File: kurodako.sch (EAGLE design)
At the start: 41 parts, among them J1 CONN-4P-MICROMATCH-SMD, J10 CONN-4P-MICROMATCH-SMD, J11 CONN-4P-MICROMATCH-SMD, J12 CONN-4P-MICROMATCH-SMD, J13 CONN-4P-MICROMATCH-SMD, J14 CONN-4P-MICROMATCH-SMD, J15 CONN-4P-MICROMATCH-SMD, J16 CONN-4P-MICROMATCH-SMD, J2 CONN-4P-MICROMATCH-SMD, J3 CONN-4P-MICROMATCH-SMD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

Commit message: Added resistors on mic high and possiblity to change pdm clk.
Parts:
- added R10, R11, R12, R13: 100, adafruit:R-US_R0805
- added R9: (no value), adafruit:R-US_R0805
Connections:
- new net DAT1_H: J1.3, J2.3, MIC1L.DAT, R10.2
- new net DAT2_H: J5.3, J6.3, MIC2L.DAT, R11.2
- new net DAT3_H: J10.3, J9.3, MIC3L.DAT, R12.2
- new net DAT4_H: J13.3, J14.3, MIC4L.DAT, R13.2
- net DAT1: now also R10.1; no longer J1.3, J2.3, MIC1L.DAT
- net DAT2: now also R11.1; no longer J5.3, J6.3, MIC2L.DAT
- net DAT3: now also R12.1; no longer J10.3, J9.3, MIC3L.DAT
- net DAT4: now also R13.1; no longer J13.3, J14.3, MIC4L.DAT
- net PDM_CLK: now also R9.1, R9.2

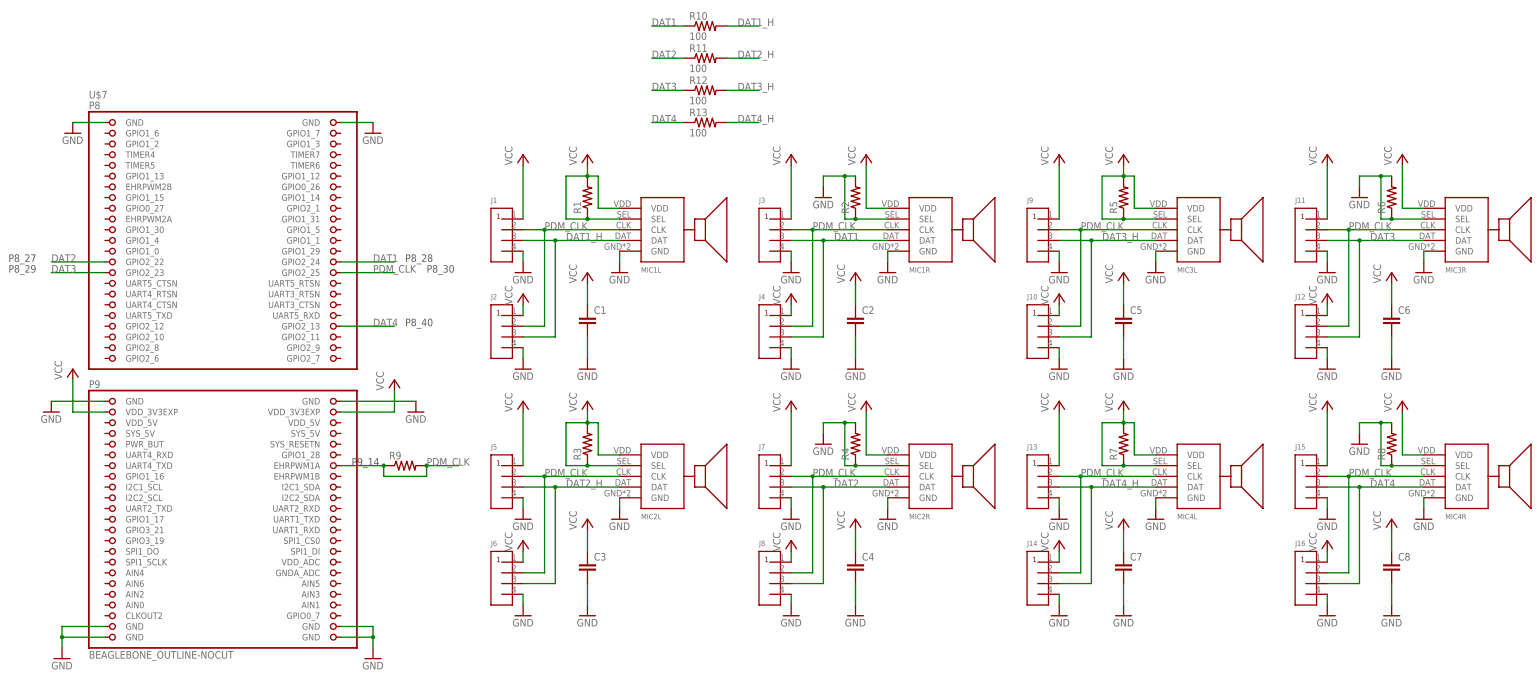
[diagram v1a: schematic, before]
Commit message: Added some values for the components on the schematics, a pdf of the schematics and the BOM.
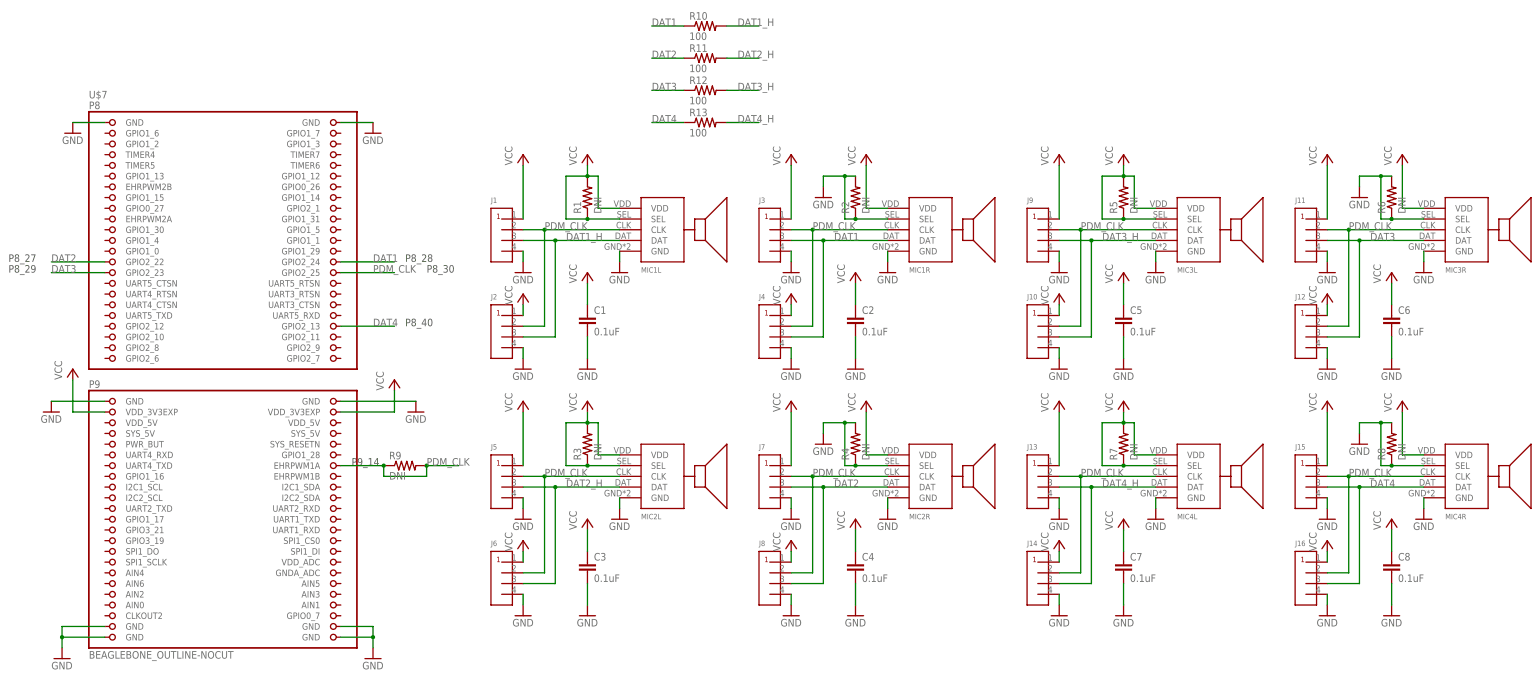
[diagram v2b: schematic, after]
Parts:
- C1, C2, C3, C4, C5, C6, C7, C8: value (none) -> 0.1uF
- R1, R2, R3, R4, R5, R6, R7, R8, R9: value (none) -> DNI
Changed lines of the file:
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@@
 <part name="J1" library="LCAV" deviceset="CONN-4P" device="-MICROMATCH-SMD"/>
 <part name="J2" library="LCAV" deviceset="CONN-4P" device="-MICROMATCH-SMD"/>
-<part name="R1" library="adafruit" deviceset="R-US_" device="R0805"/>
+<part name="R1" library="adafruit" deviceset="R-US_" device="R0805" value="DNI"/>
 <part name="GND1" library="supply1" deviceset="GND" device=""/>
 <part name="P+1" library="supply1" deviceset="VCC" device=""/>
-<part name="C1" library="SparkFun" deviceset="CAP" device="0805"/>
+<part name="C1" library="SparkFun" deviceset="CAP" device="0805" value="0.1uF"/>
 <part name="GND2" library="supply1" deviceset="GND" device=""/>
 <part name="GND4" library="supply1" deviceset="GND" device=""/>
@@
 <part name="J3" library="LCAV" deviceset="CONN-4P" device="-MICROMATCH-SMD"/>
 <part name="J4" library="LCAV" deviceset="CONN-4P" device="-MICROMATCH-SMD"/>
-<part name="R2" library="adafruit" deviceset="R-US_" device="R0805"/>
+<part name="R2" library="adafruit" deviceset="R-US_" device="R0805" value="DNI"/>
 <part name="GND3" library="supply1" deviceset="GND" device=""/>
 <part name="P+3" library="supply1" deviceset="VCC" device=""/>
-<part name="C2" library="SparkFun" deviceset="CAP" device="0805"/>
+<part name="C2" library="SparkFun" deviceset="CAP" device="0805" value="0.1uF"/>
 <part name="GND6" library="supply1" deviceset="GND" device=""/>
 <part name="GND7" library="supply1" deviceset="GND" device=""/>
@@
 <part name="J5" library="LCAV" deviceset="CONN-4P" device="-MICROMATCH-SMD"/>
 <part name="J6" library="LCAV" deviceset="CONN-4P" device="-MICROMATCH-SMD"/>
-<part name="R3" library="adafruit" deviceset="R-US_" device="R0805"/>
+<part name="R3" library="adafruit" deviceset="R-US_" device="R0805" value="DNI"/>
 <part name="GND10" library="supply1" deviceset="GND" device=""/>
 <part name="P+7" library="supply1" deviceset="VCC" device=""/>
-<part name="C3" library="SparkFun" deviceset="CAP" device="0805"/>
+<part name="C3" library="SparkFun" deviceset="CAP" device="0805" value="0.1uF"/>
 <part name="GND11" library="supply1" deviceset="GND" device=""/>
 <part name="GND12" library="supply1" deviceset="GND" device=""/>
@@
 <part name="J7" library="LCAV" deviceset="CONN-4P" device="-MICROMATCH-SMD"/>
 <part name="J8" library="LCAV" deviceset="CONN-4P" device="-MICROMATCH-SMD"/>
-<part name="R4" library="adafruit" deviceset="R-US_" device="R0805"/>
+<part name="R4" library="adafruit" deviceset="R-US_" device="R0805" value="DNI"/>
 <part name="GND14" library="supply1" deviceset="GND" device=""/>
 <part name="P+10" library="supply1" deviceset="VCC" device=""/>
-<part name="C4" library="SparkFun" deviceset="CAP" device="0805"/>
+<part name="C4" library="SparkFun" deviceset="CAP" device="0805" value="0.1uF"/>
 <part name="GND15" library="supply1" deviceset="GND" device=""/>
 <part name="GND16" library="supply1" deviceset="GND" device=""/>
@@
 <part name="J9" library="LCAV" deviceset="CONN-4P" device="-MICROMATCH-SMD"/>
 <part name="J10" library="LCAV" deviceset="CONN-4P" device="-MICROMATCH-SMD"/>
-<part name="R5" library="adafruit" deviceset="R-US_" device="R0805"/>
+<part name="R5" library="adafruit" deviceset="R-US_" device="R0805" value="DNI"/>
 <part name="GND19" library="supply1" deviceset="GND" device=""/>
 <part name="P+13" library="supply1" deviceset="VCC" device=""/>
-<part name="C5" library="SparkFun" deviceset="CAP" device="0805"/>
+<part name="C5" library="SparkFun" deviceset="CAP" device="0805" value="0.1uF"/>
 <part name="GND20" library="supply1" deviceset="GND" device=""/>
 <part name="GND21" library="supply1" deviceset="GND" device=""/>
@@
 <part name="J11" library="LCAV" deviceset="CONN-4P" device="-MICROMATCH-SMD"/>
 <part name="J12" library="LCAV" deviceset="CONN-4P" device="-MICROMATCH-SMD"/>
-<part name="R6" library="adafruit" deviceset="R-US_" device="R0805"/>
+<part name="R6" library="adafruit" deviceset="R-US_" device="R0805" value="DNI"/>
 <part name="GND23" library="supply1" deviceset="GND" device=""/>
 <part name="P+16" library="supply1" deviceset="VCC" device=""/>
-<part name="C6" library="SparkFun" deviceset="CAP" device="0805"/>
+<part name="C6" library="SparkFun" deviceset="CAP" device="0805" value="0.1uF"/>
 <part name="GND24" library="supply1" deviceset="GND" device=""/>
 <part name="GND25" library="supply1" deviceset="GND" device=""/>
@@
 <part name="J13" library="LCAV" deviceset="CONN-4P" device="-MICROMATCH-SMD"/>
 <part name="J14" library="LCAV" deviceset="CONN-4P" device="-MICROMATCH-SMD"/>
-<part name="R7" library="adafruit" deviceset="R-US_" device="R0805"/>
+<part name="R7" library="adafruit" deviceset="R-US_" device="R0805" value="DNI"/>
 <part name="GND28" library="supply1" deviceset="GND" device=""/>
 <part name="P+19" library="supply1" deviceset="VCC" device=""/>
-<part name="C7" library="SparkFun" deviceset="CAP" device="0805"/>
+<part name="C7" library="SparkFun" deviceset="CAP" device="0805" value="0.1uF"/>
 <part name="GND29" library="supply1" deviceset="GND" device=""/>
 <part name="GND30" library="supply1" deviceset="GND" device=""/>
@@
 <part name="J15" library="LCAV" deviceset="CONN-4P" device="-MICROMATCH-SMD"/>
 <part name="J16" library="LCAV" deviceset="CONN-4P" device="-MICROMATCH-SMD"/>
-<part name="R8" library="adafruit" deviceset="R-US_" device="R0805"/>
+<part name="R8" library="adafruit" deviceset="R-US_" device="R0805" value="DNI"/>
 <part name="GND32" library="supply1" deviceset="GND" device=""/>
 <part name="P+22" library="supply1" deviceset="VCC" device=""/>
-<part name="C8" library="SparkFun" deviceset="CAP" device="0805"/>
+<part name="C8" library="SparkFun" deviceset="CAP" device="0805" value="0.1uF"/>
 <part name="GND33" library="supply1" deviceset="GND" device=""/>
 <part name="GND34" library="supply1" deviceset="GND" device=""/>
@@
 <part name="P+33" library="supply1" deviceset="VCC" device=""/>
 <part name="P+34" library="supply1" deviceset="VCC" device=""/>
-<part name="R9" library="adafruit" deviceset="R-US_" device="R0805"/>
+<part name="R9" library="adafruit" deviceset="R-US_" device="R0805" value="DNI"/>
 <part name="R10" library="adafruit" deviceset="R-US_" device="R0805" value="100"/>
 <part name="R11" library="adafruit" deviceset="R-US_" device="R0805" value="100"/>
